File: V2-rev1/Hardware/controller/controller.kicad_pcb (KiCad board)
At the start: 2 copper layers, 56 parts, among them J0 Molex_PSU, J2 7SEG_12V, J3 RPI_DATA_3.3V, Q0 BD139-16, Q1 BD139-16, Q2 BD139-16, Q3 BD139-16, Q4 BD139-16, Q5 BD139-16, Q6 BD139-16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

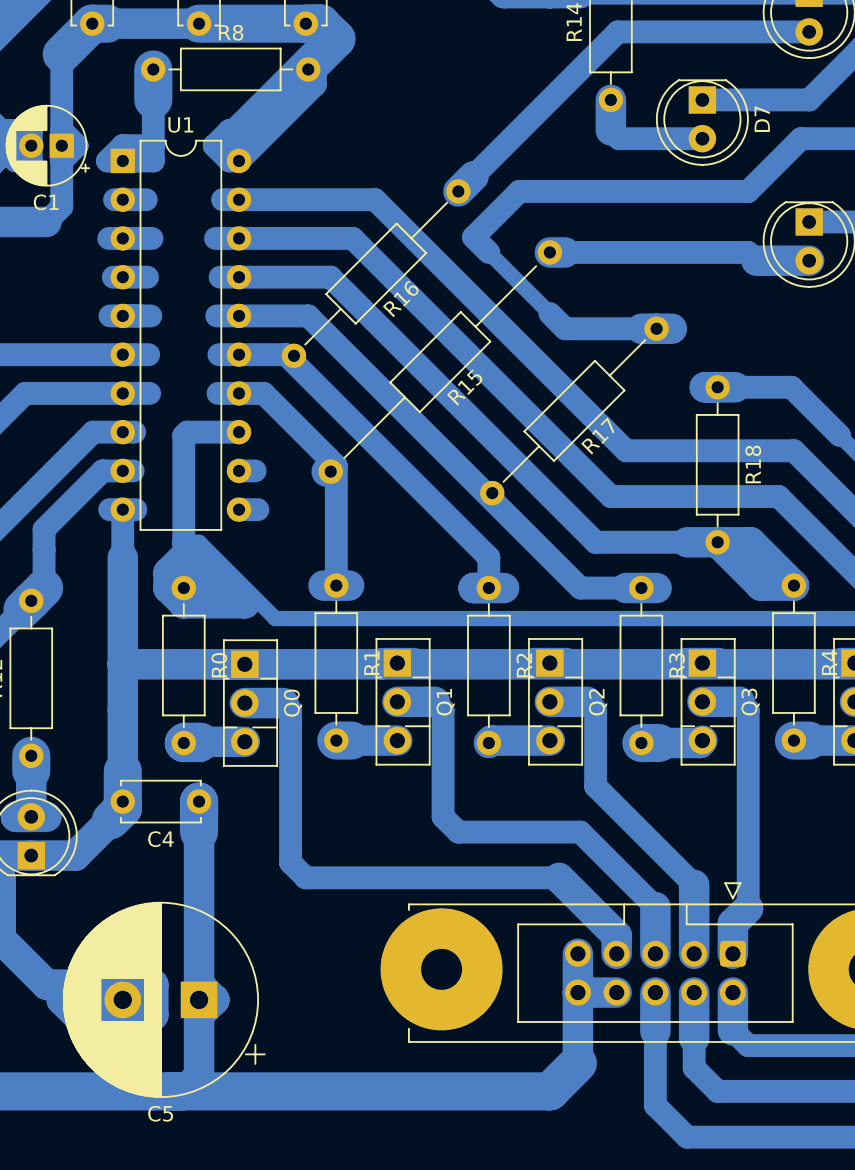
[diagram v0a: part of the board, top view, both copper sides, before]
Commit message: mark pin 1
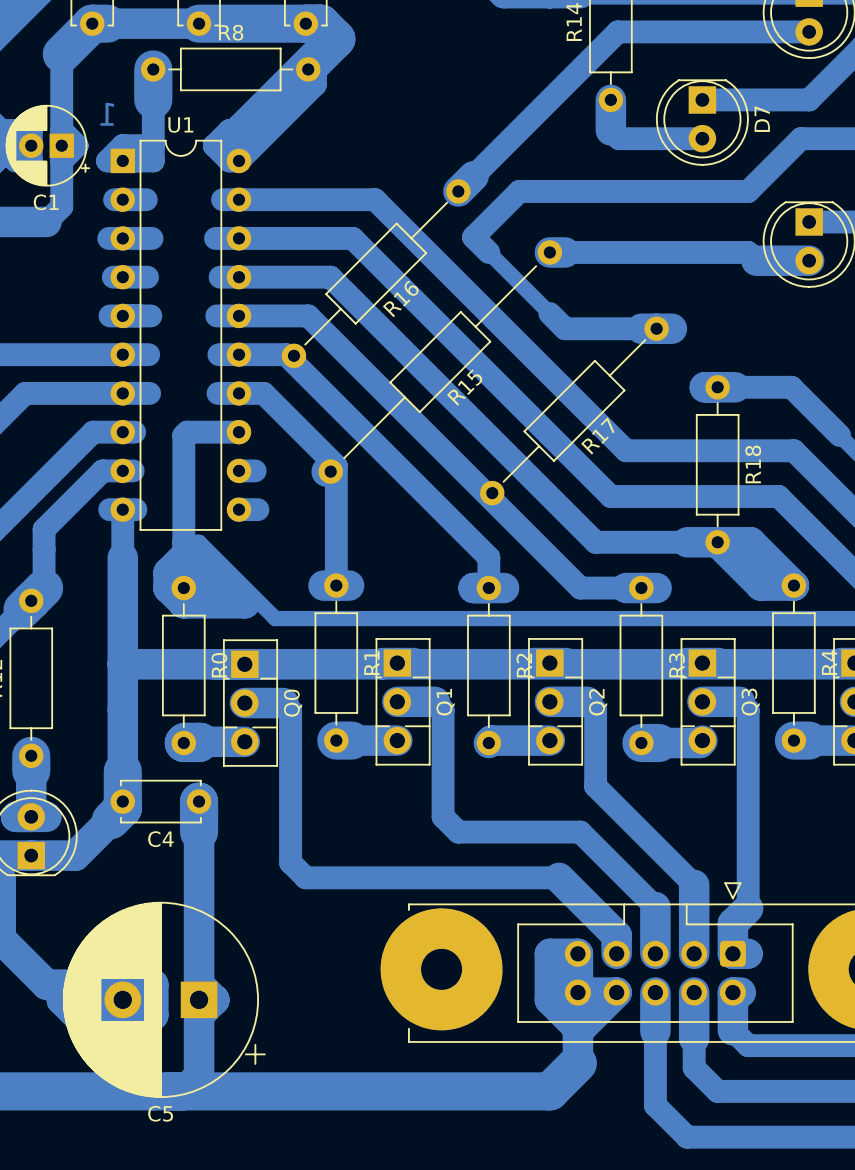
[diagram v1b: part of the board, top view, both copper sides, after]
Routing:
- net /+12V: track 256.8 -> 267.7 mm
- net /SEG_D: track 19.6 -> 20.6 mm
- net /SEG_C: track 67.3 -> 67.8 mm
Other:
- board text added: "1"

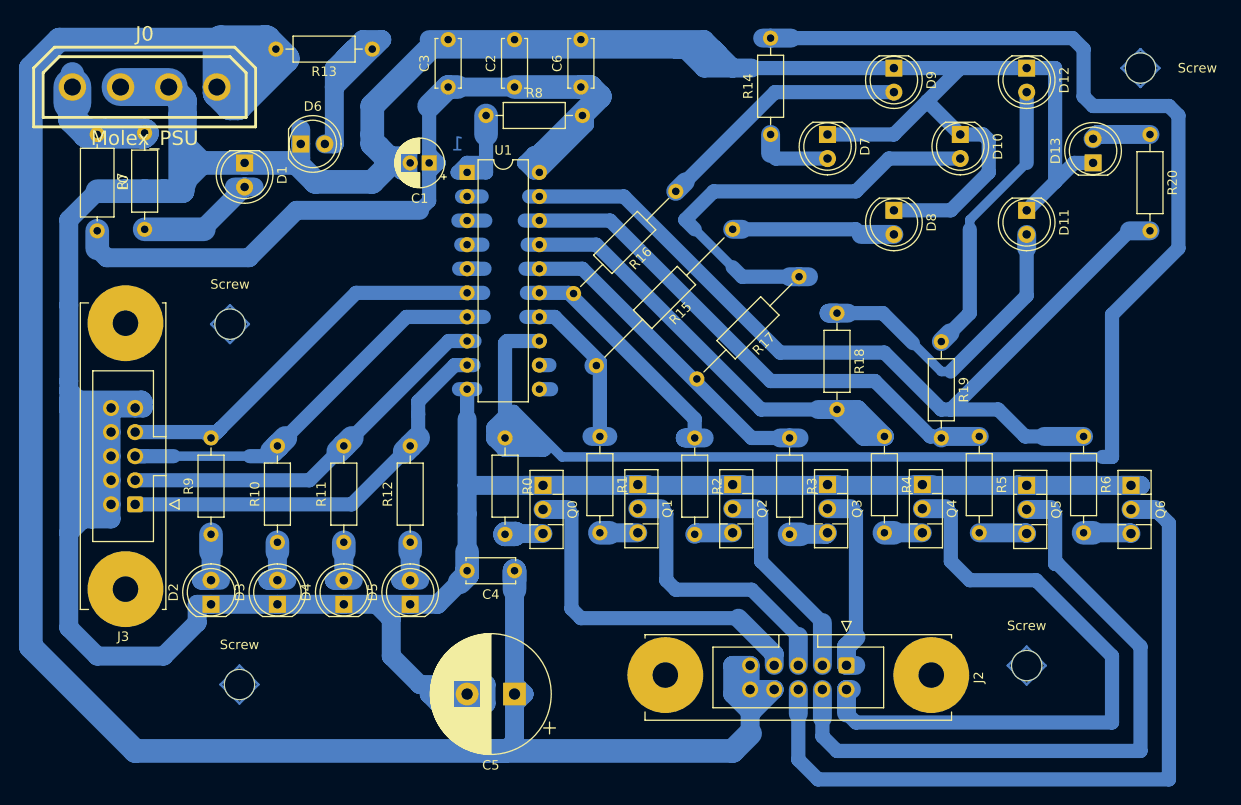
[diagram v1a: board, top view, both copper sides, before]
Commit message: reinforce some copper
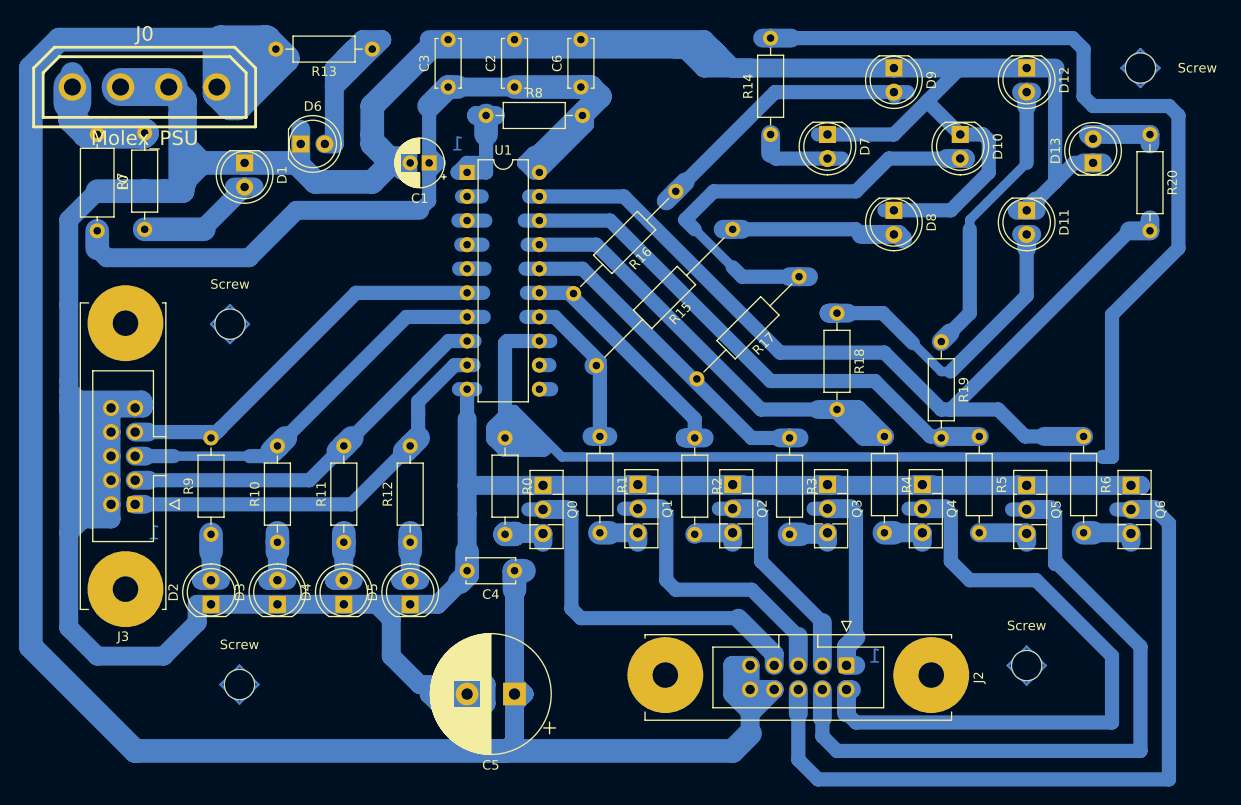
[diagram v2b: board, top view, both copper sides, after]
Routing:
- net Earth: track 601.1 -> 640.1 mm
- net Net-(D9-Pad2): track 27.3 -> 31.2 mm
- net Net-(R8-Pad1): track 14.4 -> 17.4 mm
- net Net-(D8-Pad2): track 17.2 -> 19.3 mm
- net Net-(D7-Pad2): track 8.22 -> 10.3 mm
- net /SEG_A: track 79.6 -> 81.7 mm
- net Net-(D13-Pad2): track 6.19 -> 8.11 mm
- net /SEG_G: track 37.8 -> 39.3 mm
- net /SEG_B: track 71.2 -> 72.7 mm
- net /SEG_F: track 29.7 -> 31.1 mm
- net /SEG_E: track 21.9 -> 23.3 mm
- net /SEG_D: track 20.6 -> 22.1 mm
- net /SEG_C: track 67.8 -> 69.2 mm
- net Net-(R20-Pad2): track 97.7 -> 98.9 mm
- net Net-(R0-Pad1): track 184.9 -> 186.1 mm
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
